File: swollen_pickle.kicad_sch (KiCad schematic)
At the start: 1 part, among them Q1 MBT3904DW1

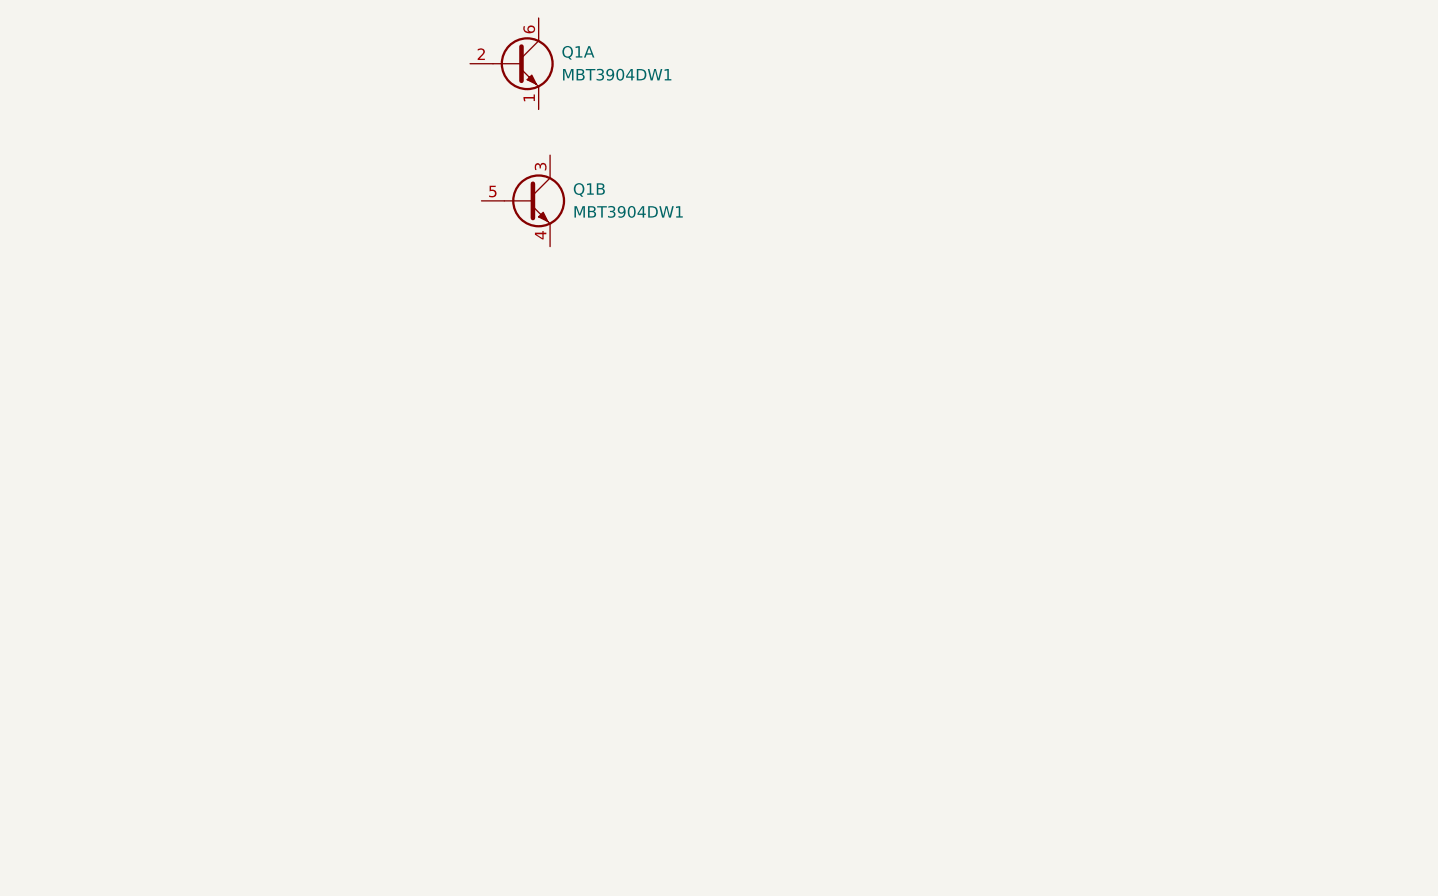
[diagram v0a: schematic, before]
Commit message: Title block change
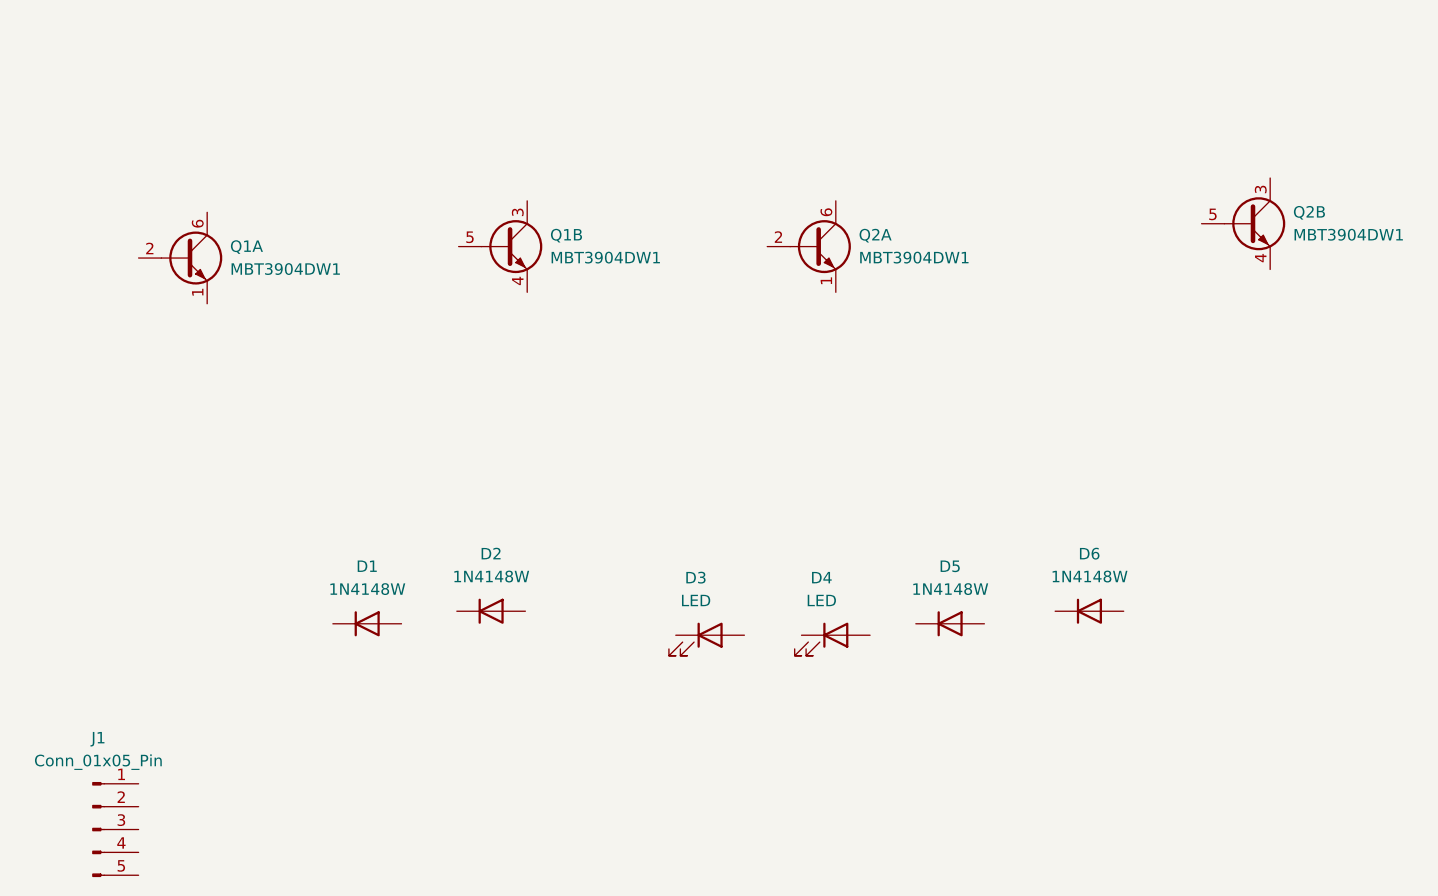
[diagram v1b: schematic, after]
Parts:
- added D1, D2, D5, D6: 1N4148W, Diode_SMD:D_SOD-123, symbol Diode:1N4148W
- added D3, D4: LED, LED_SMD:LED_2010_5025Metric, symbol Device:LED
- added J1: Conn_01x05_Pin, Connector_Molex:Molex_KK-254_AE-6410-05A_1x05_P2.54mm_Vertical, symbol Connector:Conn_01x05_Pin
- added Q2: MBT3904DW1, Package_TO_SOT_SMD:SOT-363_SC-70-6, symbol Transistor_BJT:MBT3904DW1
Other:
- moved on the sheet: Q1A, Q1B
